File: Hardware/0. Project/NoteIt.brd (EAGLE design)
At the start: 50 x 35 mm, 65 parts, among them CN1 USB 3.2 Gen 2 Type C Receptac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, CN2 Lithium Ion Polymer, CN4 FTSH-105-01-L-DV-K-TR, CN5 CR1220, CN6 Micro-SD Card, Q1 BC817, Q2 SI2374DS, Q3 SI2374DS, SW1 KY-040, U1 MCP73831/2, U2 MSP430FR2476TPTR, U3 S-8261ACMMD-G4MT2U, U4 GL823K, U5 SN74AHC1G125DBV, U6 TS3A27518EPWR, U7 TLV75530PDBVR, U8 DS3231/SO, Y1 32.768 kHz

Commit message: WIP
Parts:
- C1: value 10uF x 10V -> 10uF
- C13: value 1nF x 50V -> 1nF
- C8, C9: value 22pF x 100V -> 22pF
- R10, R19, R20: value 4K7 (5%) -> 4k7
- R13, R18, R21, R22, R23, R8: value 10k (5%) -> 10k
- R14: value 1k (5%) -> 1k
- R17: value 47k (5%) -> 47k
- R3, R6: value 5k1 (5%) -> 5k1
- R5: value 4K7 -> 4k7
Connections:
- net N$33 renamed VBAT
- net 0V: no longer CN4.7
- net USB_N: now also CN1.B7, U4.16; no longer CN1.B6, U4.15
- net USB_P: now also CN1.B6, U4.15; no longer CN1.B7, U4.16
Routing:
- net USB_N: track 11.0 -> 14.2 mm, vias 1 -> 3
- net VUSB: track 79.1 -> 78.5 mm
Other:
- board text added: "NoteIt v1.3"
- board text removed: "NoteIt v1.2"

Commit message: PCB revision WIP
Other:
- board text added: "NoteIt v2.0"
- board text removed: "NoteIt v1.3"
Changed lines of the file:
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@@
 <layer number="19" name="Unrouted" color="58" fill="1" visible="yes" active="yes"/>
 <layer number="20" name="Dimension" color="13" fill="1" visible="yes" active="yes"/>
-<layer number="21" name="tPlace" color="7" fill="1" visible="no" active="yes"/>
+<layer number="21" name="tPlace" color="7" fill="1" visible="yes" active="yes"/>
 <layer number="22" name="bPlace" color="63" fill="1" visible="yes" active="yes"/>
-<layer number="23" name="tOrigins" color="15" fill="1" visible="no" active="yes"/>
-<layer number="24" name="bOrigins" color="15" fill="1" visible="no" active="yes"/>
-<layer number="25" name="tNames" color="7" fill="1" visible="no" active="yes"/>
+<layer number="23" name="tOrigins" color="15" fill="1" visible="yes" active="yes"/>
+<layer number="24" name="bOrigins" color="15" fill="1" visible="yes" active="yes"/>
+<layer number="25" name="tNames" color="7" fill="1" visible="yes" active="yes"/>
 <layer number="26" name="bNames" color="7" fill="1" visible="yes" active="yes"/>
-<layer number="27" name="tValues" color="7" fill="1" visible="no" active="yes"/>
+<layer number="27" name="tValues" color="7" fill="1" visible="yes" active="yes"/>
 <layer number="28" name="bValues" color="7" fill="1" visible="yes" active="yes"/>
 <layer number="29" name="tStop" color="7" fill="3" visible="no" active="yes"/>
@@
 <hole x="2" y="33" drill="2"/>
 <hole x="33" y="33" drill="2"/>
-<text x="18.19148125" y="33.157159375" size="1.778" layer="21" font="vector" ratio="16" align="center">NoteIt v1.3</text>
+<text x="18.19148125" y="33.157159375" size="1.778" layer="21" font="vector" ratio="16" align="center">NoteIt v2.0</text>
 </plain>
 <attributes>

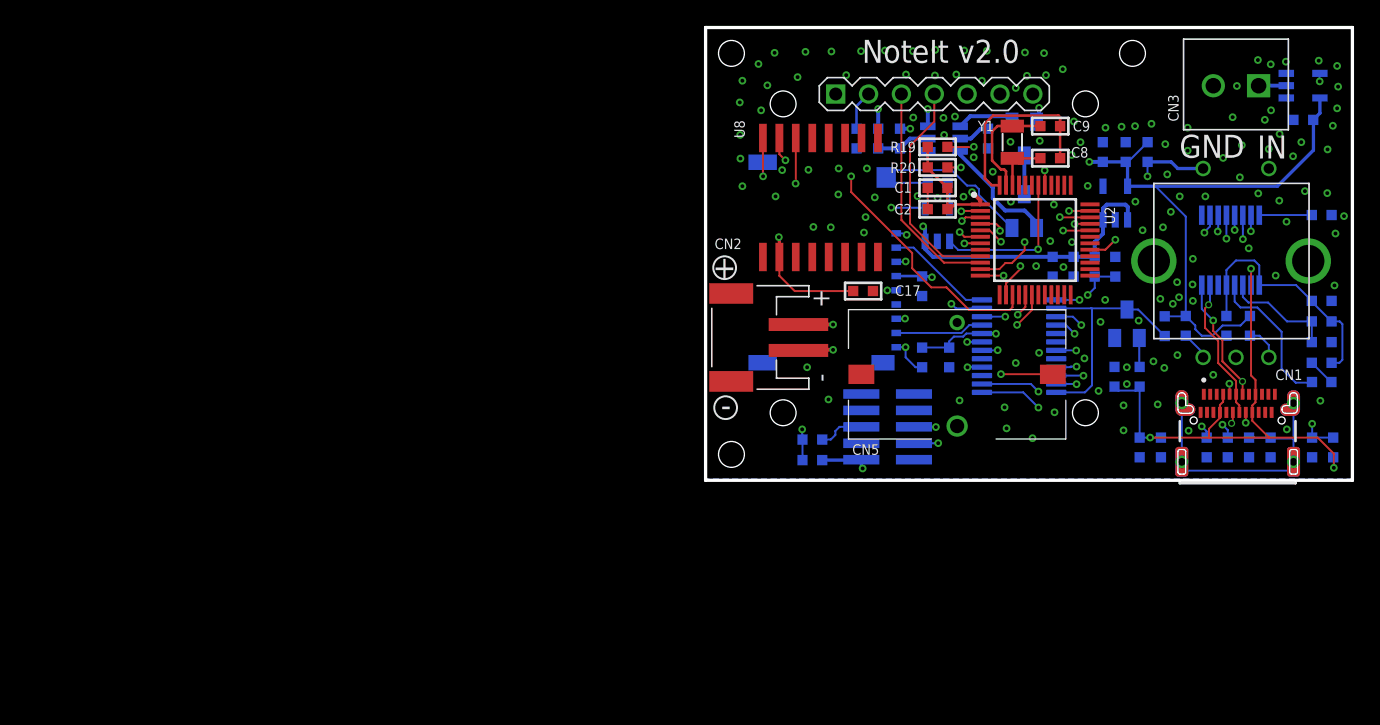
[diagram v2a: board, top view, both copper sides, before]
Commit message: Schematic minor improvements and bug fix to pre PCB v3.0 release
- Fix bug at USB DP and DN.
- Change all parts to my own libraries.
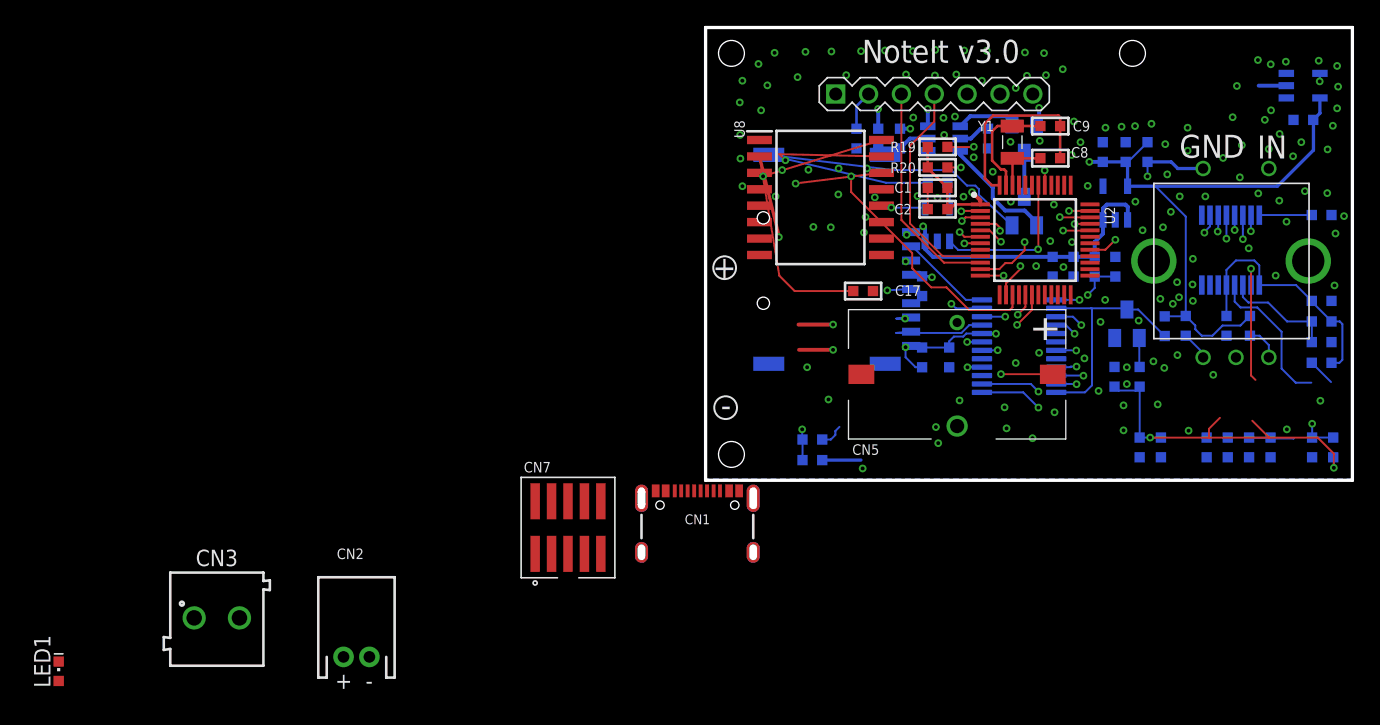
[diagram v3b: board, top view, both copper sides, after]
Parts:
- removed CN4: FTSH-105-01-L-DV-K-TR, SamacSys_Parts:FTSH10501LDVKTR
- removed DS1: DISPLAY-OLED-128X64, diy-modules:DISPLAY-OLED-128X64
- added CN7: JTAG, My-Connectors:JTAG-ARM-10P
- added CN9: OLED-MODULE-SPI-NO_HOLES, My-Displays:PIN_HEADER_1X7_NH
- CN1: value USB 3.2 Gen 2 Type C Receptacle -> USB Type C Receptacle; device USB C CONNECOTR:GCT_USB4080-03-A_REVA -> My-Connectors:USB-C-16P-2LAYER-PADS
- CN2: value Lithium Ion Polymer -> CELL-JST-PH-2P-H; device Battery:JST-PH-2-SMT-RA -> My-Battery:JST-PH-2P-H
- CN3: value (none) -> 2P-BLOCK-3.5MM-2P; device Terminal Block 2P 3.5pitch:OST_OSTTE020104 -> My-Connectors:BLOCK-3.5MM-2P
- CN5: value CR1220 -> CR-1225; device SamacSys_Parts:1072 -> My-Battery:CR1220/1225_HOLDER
- CN6: value Micro-SD Card -> Micro SD-Card; device Micro SD:MICROSD-PUSH-OUT -> My-Sockets:SD-CARD
- LED1: value (none) -> LED-0603; device led:CHIPLED_0603 -> My-LEDs:LED-0603
- Q1: device transistor-npn:SOT23-BEC -> My-Transistors:SOT23-3
- Q2, Q3: value SI2374DS -> N-FET-ENHANCEMENT-SQ2310; device SI2374DS:SOT-23(TO-236) -> My-Transistors:SOT23-3
- SW1: device rotary-encoder:KY-040 -> My-Electromechanicals:KY-040
- U1: device adafruit:SOT23-5L -> My-ICs:SOT-23-5
- U2: device MSP430FR2476TPTR:QFP50P900X900X160-48N -> My-Microcontrollers:LQFP-48
- U3: value S-8261ACMMD-G4MT2U -> S-8261; device SamacSys_Parts:SOT95P275X135-6N -> My-ICs:SOT-23-6
- U4: device SamacSys_Parts:SOP64P600X175-16N -> My-ICs:SSOP16
- U5: value SN74AHC1G125DBV -> SN74AHC1G125; device SN74AHC1G125DRLR:SOT23-5 -> My-ICs:SOT-23-5
- U6: value TS3A27518EPWR -> TS3A27518E; device TS3A27518EPWR:SOP65P640X120-24N -> My-ICs:TSSOP-24
- U7: device TLV75530PDBVR:SOT23-5L -> My-LDOs:SOT-23-5
- U8: value DS3231/SO -> DS3231-SO16; device adafruit:SO16W -> My-ICs:SOIC-16W_(SO16)
- Y1: device crystal-geyer_V1_0:3.2X1.5 -> My-Crystals:3.2MM_1.6MM
- moved LED1 100.2 mm to (-50.0, -14.8), flipped to the top, turned to 0 degrees
- moved CN3 88.9 mm to (-37.8, -10.6), turned to 0 degrees
- moved CN1 42.3 mm to (-0.64, -0.48)
- moved CN2 39.2 mm to (-27.0, -13.7), turned to 0 degrees
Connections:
- net USB_N renamed N$18
- net USB_P renamed N$17
- removed net N$21: CN1.B5, R6.1
- new net N$19: CN1.A5, R6.1
- net !CONNECT_SDCARD_TO_USB: now also Q1.3; no longer Q1.C
- net !GPIO_DISPLAY_RESET: now also CN9.5; no longer DS1.5
- net !SDCARD_CARD_DETECT!: now also CN6.P9; no longer CN6.9
- net !SPI_DISPLAY_CS: now also CN9.7; no longer DS1.7
- net 0V: now also CN1.GND, CN1.GND2, CN6.MP1, CN6.MP2, CN6.MP3, CN6.MP4, CN6.P6, CN7.3, CN7.5, CN7.9, CN9.1, Q1.2; no longer CN1.A1, CN1.A12, CN1.B1, CN1.B12, CN4.3, CN4.5, CN4.9, CN6.6, CN6.G1, CN6.G2, CN6.G3, CN6.G4, DS1.1, Q1.E
- net 3.3V: now also CN6.P4, CN7.1, CN9.2; no longer CN4.1, CN6.4, DS1.2
- net GPIO_DISPLAY_TRANSMISSION_MODE: now also CN9.6; no longer DS1.6
- net ICSP_SBWTCK: now also CN7.4; no longer CN4.4
- net ICSP_SBWTDIO: now also CN7.6; no longer CN4.6
- net N$10: now also CN1.SHLD1, CN1.SHLD2, CN1.SHLD3, CN1.SHLD4; no longer CN1.G1, CN1.G2, CN1.G3, CN1.G4
- net N$14: now also Q1.1; no longer Q1.B
- net N$15: now also CN6.P3; no longer CN6.3
- net N$16: now also CN6.P7; no longer CN6.7
- net N$2: now also CN6.P5; no longer CN6.5
- net N$20: now also CN6.P8; no longer CN6.8
- net N$6: now also CN1.B5; no longer CN1.A5
- net N$7: now also CN6.P1; no longer CN6.1
- net N$8: now also CN6.P2; no longer CN6.2
- net SPI_DISPLAY_SCLK: now also CN9.3; no longer DS1.3
- net SPI_DISPLAY_SIMO: now also CN9.4; no longer DS1.4
- net VUSB: now also CN1.VBUS1, CN1.VBUS2; no longer CN1.A4, CN1.A9, CN1.B4, CN1.B9
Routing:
- net N$10: track 22.6 -> 3.47 mm
- net 0V: track 35.8 -> 51.8 mm
- net N$18: track 14.2 -> 0.00 mm, vias 3 -> 0
- net 3.3V: track 180.3 -> 191.4 mm
- net N$17: track 11.1 -> 0.00 mm, vias 1 -> 0
- net I2C_RTC_SDA: track 32.4 -> 39.0 mm
- net I2C_RTC_SCL: track 38.8 -> 45.4 mm
- net N$21: track 5.72 -> 0.00 mm, vias 2 -> 0
- net N$6: track 5.38 -> 0.00 mm, vias 2 -> 0
- net VUSB: track 78.5 -> 73.3 mm
- net N$22: track 36.4 -> 39.5 mm
- net ICSP_SBWTCK: track 21.4 -> 19.5 mm
- net ICSP_SBWTDIO: track 33.5 -> 31.8 mm
- net N$2: track 13.7 -> 14.9 mm
- net N$20: track 6.88 -> 8.03 mm
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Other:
- board text added: ">VERSION"
- board text removed: "NoteIt v2.0"

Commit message: PCB v2.0 release
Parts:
- removed CN9: OLED-MODULE-SPI-NO_HOLES, My-Displays:PIN_HEADER_1X7_NH
- added CN4: JTAG, My-Connectors:JTAG-ARM-10P
- CN7: value JTAG -> OLED-MODULE-SPI-NO_HOLES; device My-Connectors:JTAG-ARM-10P -> My-Displays:PIN_HEADER_1X7_NH
- R10: value 4k7 -> 470R
- R3: value 5k1 -> 4k7
- R5: value 4k7 -> 5k1
- R9: value 470R -> 4k7
- moved LED1 98.3 mm to (45.2, 9.82), flipped to the bottom
- moved CN3 88.8 mm to (41.0, 30.5), turned to 180 degrees
- moved CN1 42.6 mm to (41.3, 6.83)
- moved CN7 35.1 mm to (17.7, 17.2)
- moved CN2 34.5 mm to (3.36, 2.69)
- moved R3 30.4 mm to (17.9, 23.0), turned to 180 degrees
- moved R5 30.4 mm to (40.4, 2.54), turned to 270 degrees
- moved R10 26.1 mm to (15.0, 26.4)
- moved R9 26.1 mm to (33.6, 8.00)
- moved CN6 0.92 mm to (7.78, 16.2)
- moved R18 0.53 mm to (17.3, 9.50)
- moved C20 0.51 mm to (17.2, 15.0)
- moved C13 0.50 mm to (7.76, 3.15)
- moved R17 0.50 mm to (7.76, 1.56)
- moved U8 0.16 mm to (8.82, 21.7), turned to 90 degrees
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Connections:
- net !GPIO_DISPLAY_RESET: now also CN7.5; no longer CN9.5
- net !SPI_DISPLAY_CS: now also CN7.7; no longer CN9.7
- net 0V: now also CN4.3, CN4.5, CN4.9, CN7.1, R3.1, R5.2; no longer CN7.3, CN7.5, CN7.9, CN9.1, R3.2, R5.1
- net 3.3V: now also CN4.1, CN7.2; no longer CN7.1, CN9.2
- net GPIO_DISPLAY_TRANSMISSION_MODE: now also CN7.6; no longer CN9.6
- net ICSP_SBWTCK: now also CN4.4; no longer CN7.4
- net ICSP_SBWTDIO: now also CN4.6; no longer CN7.6
- net N$14: now also R9.1; no longer R10.1
- net N$26: now also R3.2; no longer R5.2
- net N$31: now also R10.2; no longer R9.2
- net N$6: now also R5.1; no longer R3.1
- net SPI_DISPLAY_SCLK: now also CN7.3; no longer CN9.3
- net SPI_DISPLAY_SIMO: now also CN7.4; no longer CN9.4
- net VBAT: now also R10.1; no longer R9.1
- net VUSB: now also R9.2; no longer R10.2
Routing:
- net N$10: track 3.47 -> 20.6 mm
- net 0V: track 51.8 -> 35.2 mm, vias 138 -> 103
- net VBAT: track 47.4 -> 63.8 mm
- net VUSB: track 73.3 -> 88.0 mm, vias 4 -> 6
- net 3.3V: track 191.4 -> 177.1 mm
- net N$17: track 0.00 -> 13.2 mm, vias 0 -> 1
- net N$18: track 0.00 -> 11.6 mm, vias 0 -> 1
- net N$32: track 40.0 -> 50.8 mm
- net N$6: track 0.00 -> 5.47 mm, vias 0 -> 1
- net N$5: track 11.5 -> 7.31 mm
- net N$19: track 0.00 -> 4.03 mm, vias 0 -> 1
- net I2C_RTC_SCL: track 45.4 -> 41.6 mm
- net ICSP_SBWTDIO: track 31.8 -> 34.8 mm
- net UART_DATALOGGER_RX: track 23.8 -> 26.8 mm
- net I2C_RTC_SDA: track 39.0 -> 36.2 mm
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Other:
- board text removed: "+"
- board text removed: "-"
